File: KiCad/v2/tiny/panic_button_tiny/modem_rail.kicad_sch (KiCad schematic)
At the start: 1 part, among them U4 TPS61022

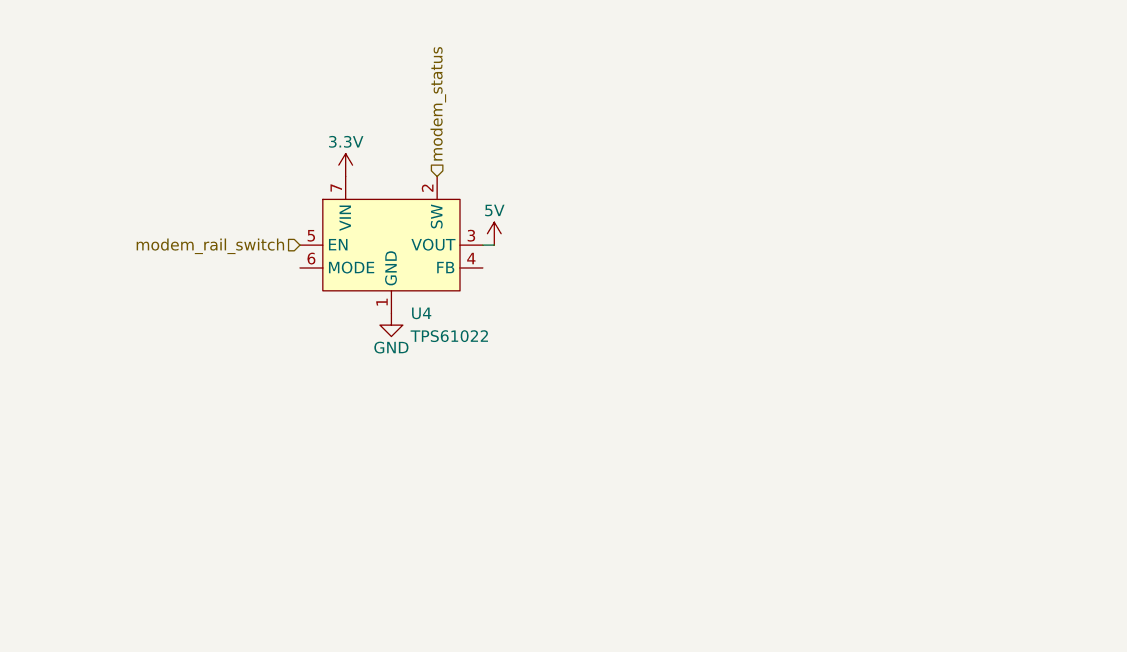
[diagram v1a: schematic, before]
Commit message: [UPDATE] connections in the schematic to better represent the logic flow
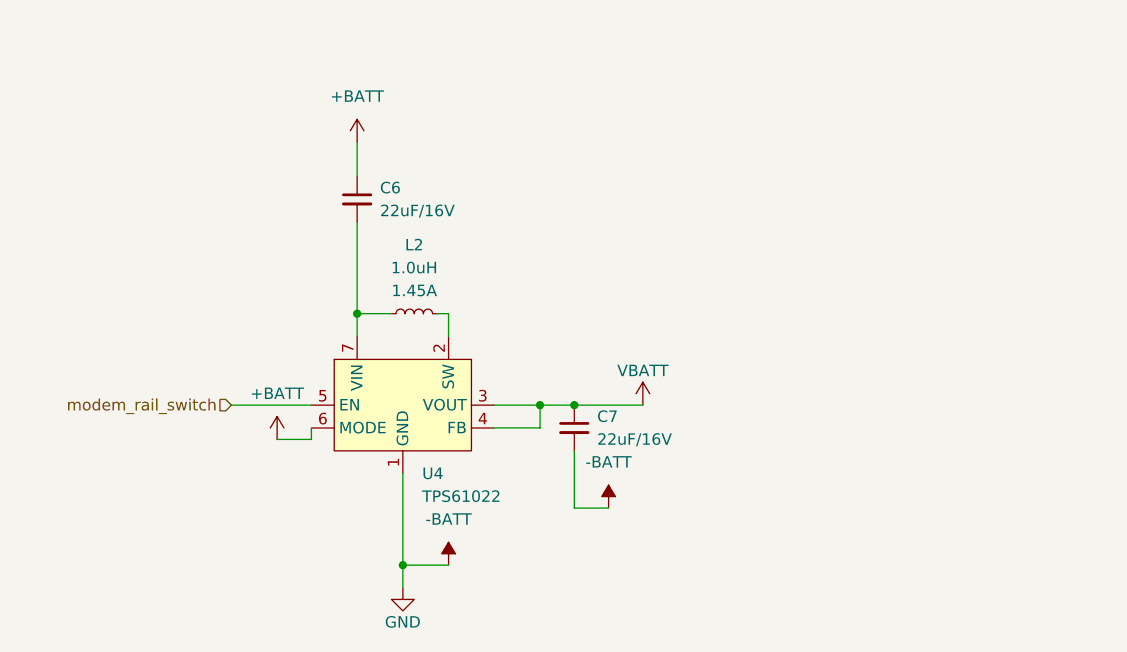
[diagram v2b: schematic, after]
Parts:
- added C6: 22uF_0603_16V, Capacitor_SMD:C_0603_1608Metric_Pad1.08x0.95mm_HandSolder, symbol PCM_4ms_Capacitor:22uF_0603_16V
- added C7: 22uF_0603_16V, 4ms_Capacitor:C_0805, symbol PCM_4ms_Capacitor:22uF_0603_16V
- added L2: 1.0uH, PCM_SparkFun-Coil:0805, symbol PCM_SparkFun-Coil:1.0uH_0805_1.45A
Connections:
- net 5V is gone; now on net VBATT: U4.3 (VOUT)
- net VBATT: now reaches U4.4 (FB)
- net VBATT: now also C7.1
- net +BATT: now reaches U4.6 (MODE)
- net +BATT: now also C6.1
- net 3.3V: no longer names the net of U4.7 (VIN)
- net 3.3V: now also C6.2, L2.1
- net GND renamed -BATT
- net -BATT: now also C7.2
- net modem_status: no longer names the net of U4.2 (SW)
- net modem_status: now also L2.2
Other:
- moved on the sheet: U4

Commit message: [UPDATE] the schematic with the connections
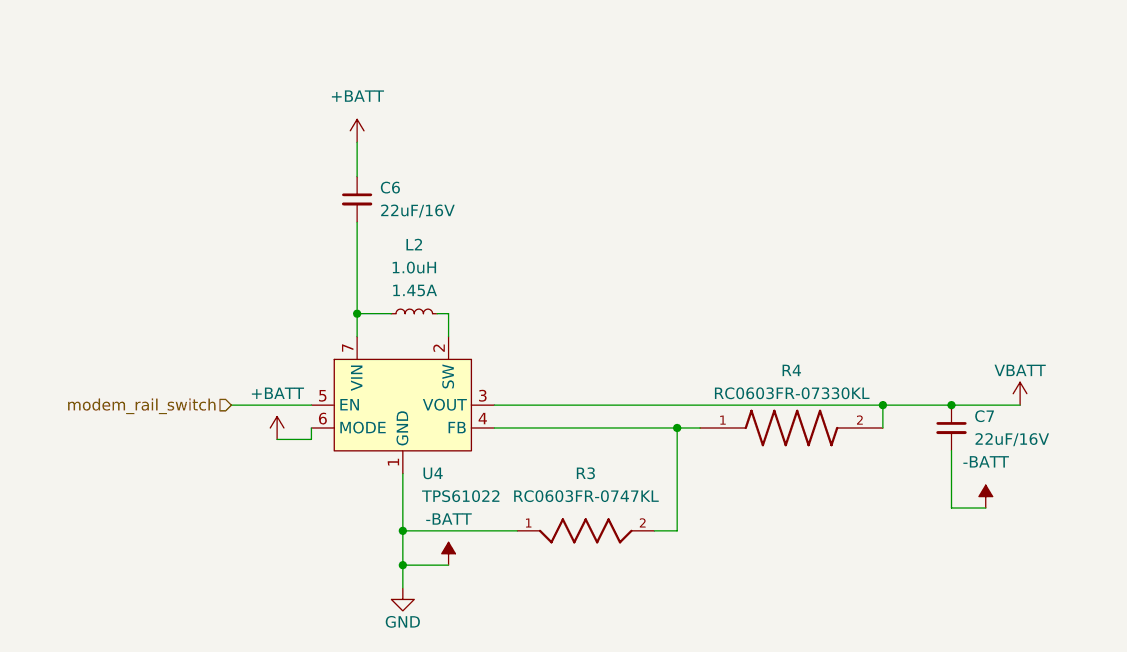
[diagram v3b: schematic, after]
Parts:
- added R3: RC0603FR-0747KL, RC0603FR-0747KL:RESC1608X55, symbol RC0603FR-0747KL:RC0603FR-0747KL
- added R4: RC0603FR-07330KL, RC0603FR-07_330KL:RESC1608X55N, symbol RC0603FR-07330KL:RC0603FR-07330KL
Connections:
- net -BATT: now also R3.1
- net VBATT: now also R4.2; no longer U4.4 (FB)
- new net: R3.2, R4.1, U4.4 (FB)
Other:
- moved on the sheet: C7

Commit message: [FIX] connection issues in the modem_rail circuit
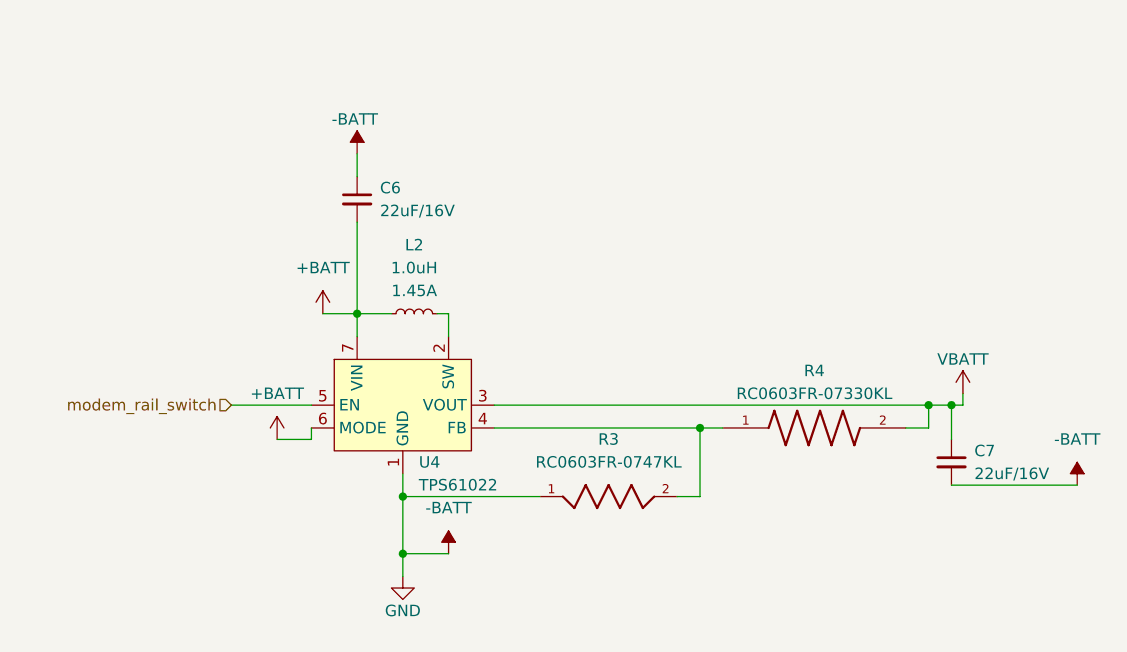
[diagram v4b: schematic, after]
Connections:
- net +BATT: now also C6.2, L2.1, U4.7 (VIN); no longer C6.1
- net -BATT: now also C6.1
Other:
- moved on the sheet: C7, R3, R4

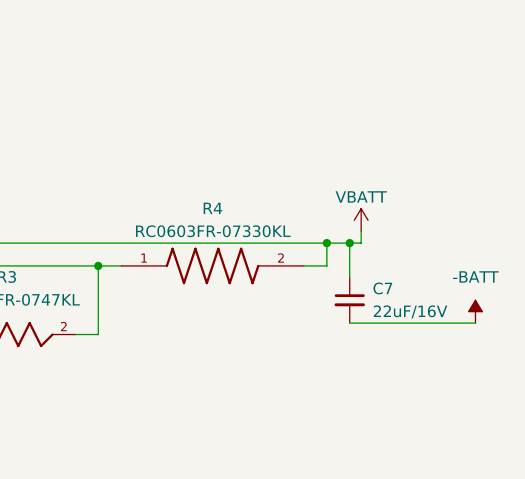
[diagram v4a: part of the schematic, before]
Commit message: [UPDATE] the schematics to hopefully include better connections
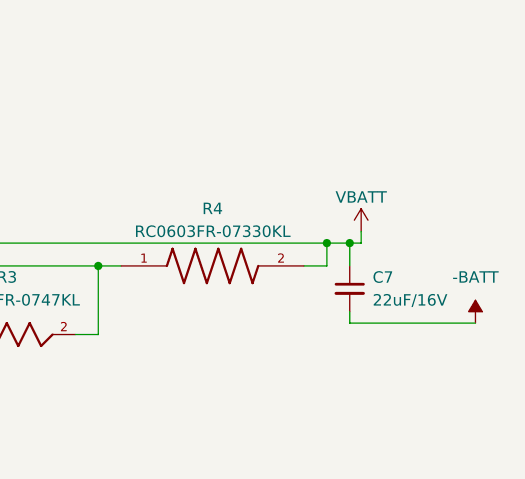
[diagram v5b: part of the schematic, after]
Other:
- moved on the sheet: C7
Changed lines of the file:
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@@
+	(wire
+		(pts
+			(xy 113.03 57.15) (xy 113.03 55.88)
+		)
+		(stroke
+			(width 0)
+			(type default)
+		)
+	)
 	(wire
 		(pts
@@
 	(wire
 		(pts
-			(xy 113.03 52.07) (xy 113.03 48.26)
+			(xy 113.03 50.8) (xy 113.03 48.26)
 		)
 		(stroke
@@
 	(wire
 		(pts
+			(xy 113.03 57.15) (xy 127 57.15)
+		)
+		(stroke
+			(width 0)
+			(type default)
+		)
+	)
+	(wire
+		(pts
 			(xy 57.15 38.1) (xy 57.15 40.64)
-		)
-		(stroke
-			(width 0)
-			(type default)
-		)
-	)
-	(wire
-		(pts
-			(xy 127 57.15) (xy 113.03 57.15)
 		)
 		(stroke
@@
 	(symbol
 		(lib_id "PCM_4ms_Capacitor:22uF_0603_16V")
-		(at 113.03 54.61 0)
+		(at 113.03 53.34 0)
 		(unit 1)
 		(body_style 1)
@@
 		(fields_autoplaced yes)
 		(property "Reference" "C7"
-			(at 115.57 53.3462 0)
+			(at 115.57 52.0762 0)
 			(show_name no)
 			(do_not_autoplace no)
@@
 		)
 		(property "Value" "22uF_0603_16V"
-			(at 113.03 50.8 0)
+			(at 113.03 49.53 0)
 			(hide yes)
 			(show_name no)
@@
 		)
 		(property "Footprint" "4ms_Capacitor:C_0805"
-			(at 110.49 59.69 0)
+			(at 110.49 58.42 0)
 			(hide yes)
 			(show_name no)
@@
 		)
 		(property "Datasheet" ""
-			(at 113.03 54.61 0)
+			(at 113.03 53.34 0)
 			(hide yes)
 			(show_name no)
@@
 		)
 		(property "Description" "22uF, 16V,10%,X5R or X7R,0603"
-			(at 113.03 54.61 0)
+			(at 113.03 53.34 0)
 			(hide yes)
 			(show_name no)
@@
 		)
 		(property "Specifications" "22uF, 16V,10%,X5R or X7R,0603"
-			(at 110.49 62.484 0)
+			(at 110.49 61.214 0)
 			(hide yes)
 			(show_name no)
@@
 		)
 		(property "Manufacturer" "Murata"
-			(at 110.49 64.008 0)
+			(at 110.49 62.738 0)
 			(hide yes)
 			(show_name no)
@@
 		)
 		(property "Part Number" "GRM219R61C226ME15K"
-			(at 110.49 65.532 0)
+			(at 110.49 64.262 0)
 			(hide yes)
 			(show_name no)
@@
 		)
 		(property "Display" "22uF/16V"
-			(at 115.57 55.8862 0)
+			(at 115.57 54.6162 0)
 			(show_name no)
 			(do_not_autoplace no)
@@
 		(dnp no)
 		(fields_autoplaced yes)
-		(property "Reference" "#PWR054"
+		(property "Reference" "#PWR055"
 			(at 127 60.96 0)
 			(hide yes)
@@
 			(project "panic_button_tiny"
 				(path "/c4eb92e9-b42f-4db0-b1d9-0ef70f7ca601/5fcd7ab2-c492-450d-9345-ebba8273bb1f"
-					(reference "#PWR054")
+					(reference "#PWR055")
 					(unit 1)
 				)
@@
 		(dnp no)
 		(fields_autoplaced yes)
-		(property "Reference" "#PWR052"
+		(property "Reference" "#PWR053"
 			(at 57.15 68.58 0)
 			(hide yes)
@@
 			(project "panic_button_tiny"
 				(path "/c4eb92e9-b42f-4db0-b1d9-0ef70f7ca601/5fcd7ab2-c492-450d-9345-ebba8273bb1f"
-					(reference "#PWR052")
+					(reference "#PWR053")
 					(unit 1)
 				)
@@
 		(in_pos_files yes)
 		(dnp no)
-		(property "Reference" "#PWR055"
+		(property "Reference" "#PWR051"
 			(at 46.99 24.13 0)
 			(hide yes)
@@
 			(project "panic_button_tiny"
 				(path "/c4eb92e9-b42f-4db0-b1d9-0ef70f7ca601/5fcd7ab2-c492-450d-9345-ebba8273bb1f"
-					(reference "#PWR055")
+					(reference "#PWR051")
 					(unit 1)
 				)
@@
 		(dnp no)
 		(fields_autoplaced yes)
-		(property "Reference" "#PWR051"
+		(property "Reference" "#PWR052"
 			(at 52.07 73.66 0)
 			(hide yes)
@@
 			(project "panic_button_tiny"
 				(path "/c4eb92e9-b42f-4db0-b1d9-0ef70f7ca601/5fcd7ab2-c492-450d-9345-ebba8273bb1f"
-					(reference "#PWR051")
+					(reference "#PWR052")
 					(unit 1)
 				)
@@
 		(dnp no)
 		(fields_autoplaced yes)
-		(property "Reference" "#PWR053"
+		(property "Reference" "#PWR054"
 			(at 114.3 50.8 0)
 			(hide yes)
@@
 			(project "panic_button_tiny"
 				(path "/c4eb92e9-b42f-4db0-b1d9-0ef70f7ca601/5fcd7ab2-c492-450d-9345-ebba8273bb1f"
-					(reference "#PWR053")
+					(reference "#PWR054")
 					(unit 1)
 				)
